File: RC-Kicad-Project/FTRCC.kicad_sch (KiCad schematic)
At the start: 12 parts, among them U1 NE555D, U2 NE555D

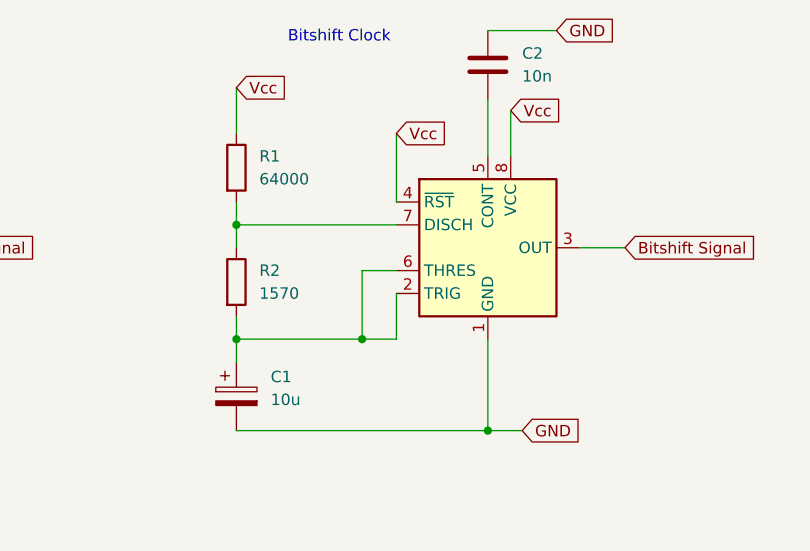
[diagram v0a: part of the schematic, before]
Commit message: update schematic and blueprint
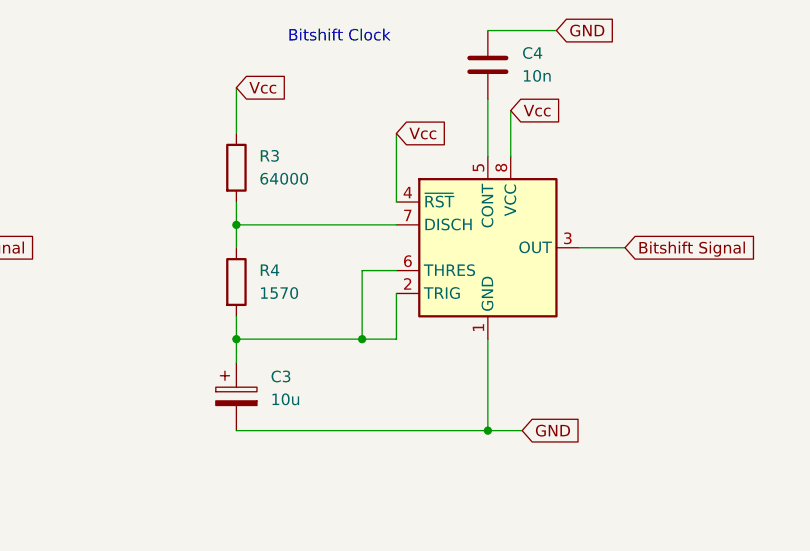
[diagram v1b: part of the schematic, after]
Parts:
- C1, C2: footprint (none) -> Capacitor_THT:CP_Radial_D10.0mm_P5.00mm
- C3: renamed from C1; footprint (none) -> Capacitor_THT:CP_Radial_D10.0mm_P5.00mm
- C4: renamed from C2; footprint (none) -> Capacitor_THT:CP_Radial_D10.0mm_P5.00mm
- renumbered R1 to R3, R2 to R4
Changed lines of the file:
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@@
 		(dnp no)
 		(fields_autoplaced yes)
-		(property "Reference" "C1"
+		(property "Reference" "C3"
 			(at 118.11 65.1509 0)
 			(effects
@@
 			)
 		)
-		(property "Footprint" ""
+		(property "Footprint" "Capacitor_THT:CP_Radial_D10.0mm_P5.00mm"
 			(at 115.2652 71.12 0)
 			(effects
@@
 			(project "FTRCC"
 				(path "/fde0babc-3fae-43b2-819e-285fe496d1b0"
-					(reference "C1")
+					(reference "C3")
 					(unit 1)
 				)
@@
 			)
 		)
-		(property "Footprint" ""
+		(property "Footprint" "Capacitor_THT:CP_Radial_D10.0mm_P5.00mm"
 			(at 33.9852 71.12 0)
 			(effects
@@
 			)
 		)
-		(property "Footprint" ""
+		(property "Footprint" "Capacitor_THT:CP_Radial_D10.0mm_P5.00mm"
 			(at 61.9252 34.29 0)
 			(effects
@@
 		(dnp no)
 		(fields_autoplaced yes)
-		(property "Reference" "C2"
+		(property "Reference" "C4"
 			(at 146.05 29.2099 0)
 			(effects
@@
 			)
 		)
-		(property "Footprint" ""
+		(property "Footprint" "Capacitor_THT:CP_Radial_D10.0mm_P5.00mm"
 			(at 143.2052 34.29 0)
 			(effects
@@
 			(project "FTRCC"
 				(path "/fde0babc-3fae-43b2-819e-285fe496d1b0"
-					(reference "C2")
+					(reference "C4")
 					(unit 1)
 				)
@@
 		(dnp no)
 		(fields_autoplaced yes)
-		(property "Reference" "R2"
+		(property "Reference" "R4"
 			(at 116.84 53.3399 0)
 			(effects
@@
 			(project "FTRCC"
 				(path "/fde0babc-3fae-43b2-819e-285fe496d1b0"
-					(reference "R2")
+					(reference "R4")
 					(unit 1)
 				)
@@
 		(on_board yes)
 		(dnp no)
-		(property "Reference" "R1"
+		(property "Reference" "R3"
 			(at 116.84 40.6399 0)
 			(effects
@@
 			(project "FTRCC"
 				(path "/fde0babc-3fae-43b2-819e-285fe496d1b0"
-					(reference "R1")
-					(unit 1)
-				)
+					(reference "R3")
+					(unit 1)
+				)
